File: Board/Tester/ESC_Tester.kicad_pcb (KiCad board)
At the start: 2 copper layers, 40 x 50 mm, 12 parts, among them P1 CONN_01X02, P2 CONN_BLDC, P3 CONN_ISP, P4 CONN_SPI, P5 CONN_PPM, U1 LM7805CT

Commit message: Work in Progress
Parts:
- turned P1 to 270 degrees
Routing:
- net GND: track 21.5 -> 12.1 mm
- net Net-(C1-Pad1): track 30.1 -> 31.6 mm
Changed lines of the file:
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@@
     (links 26)
     (no_connects 0)
-    (area 120.45 48.23736 165.17554 110.33724)
+    (area 120.196 48.23736 165.17554 110.33724)
     (thickness 1.6)
     (drawings 2)
-    (tracks 76)
+    (tracks 77)
     (zones 0)
     (modules 12)
@@
     (pad_to_mask_clearance 0.2)
     (aux_axis_origin 0 0)
-    (visible_elements FFFFFF7F)
+    (visible_elements 7FFFFFFF)
     (pcbplotparams
       (layerselection 0x00000_80000000)
@@
   )
   (module w_conn_kk100:kk100_22-23-2021 (layer F.Cu)
-    (at 126.492 93.98 90)
+    (at 126.492 93.98 270)
     (descr "2 pin vert. connector, Molex KK100 series")
-    (fp_text reference P1 (at 0 -4.318 90) (layer F.SilkS)
-      (effects (font (thickness 0.3048)))
-    )
-    (fp_text value CONN_01X02 (at 0 4.572 90) (layer F.SilkS)
+    (fp_text reference P1 (at 0 -4.318 270) (layer F.SilkS)
+      (effects (font (thickness 0.3048)))
+    )
+    (fp_text value CONN_01X02 (at 0 4.572 270) (layer F.SilkS)
       (effects (font (thickness 0.3048)))
     )
@@
     (fp_line (start -2.54 3.175) (end -2.54 -3.175) (layer F.SilkS) (width 0.254))
     (fp_line (start -2.54 -3.175) (end 2.54 -3.175) (layer F.SilkS) (width 0.254))
-    (pad 1 thru_hole rect (at -1.27 -0.0762 90) (size 1.524 2.1971) (drill 1.016) (layers *.Cu *.Mask F.SilkS)
+    (pad 1 thru_hole rect (at -1.27 -0.0762 270) (size 1.524 2.1971) (drill 1.016) (layers *.Cu *.Mask F.SilkS)
       (net 1 "Net-(C1-Pad1)"))
-    (pad 2 thru_hole oval (at 1.27 -0.0762 90) (size 1.524 2.1971) (drill 1.016) (layers *.Cu *.Mask F.SilkS)
+    (pad 2 thru_hole oval (at 1.27 -0.0762 270) (size 1.524 2.1971) (drill 1.016) (layers *.Cu *.Mask F.SilkS)
       (net 2 GND))
     (model walter/conn_kk100/22-23-2021.wrl
@@
     (effects (font (size 1.5 1.5) (thickness 0.3)) (justify mirror))
   )
-  (gr_text + (at 126.238 99.06) (layer B.Cu)
+  (gr_text + (at 125.222 89.154) (layer B.Cu)
     (effects (font (size 3 3) (thickness 0.5)) (justify mirror))
   )
+  (segment (start 126.5682 92.71) (end 129.794 92.71) (width 0.5) (layer B.Cu) (net 1) (status 400000))
+  (segment (start 132.064 94.98) (end 135.636 94.98) (width 0.5) (layer B.Cu) (net 1) (status 800000))
+  (segment (start 129.794 92.71) (end 132.064 94.98) (width 0.5) (layer B.Cu) (net 1))
+  (segment (start 126.9398 92.726) (end 126.6698 92.456) (width 0.25) (layer F.Cu) (net 1) (status 30))
   (segment (start 152.908 99.06) (end 149.86 99.06) (width 0.5) (layer B.Cu) (net 1))
   (segment (start 149.86 99.06) (end 147.828 97.028) (width 0.5) (layer B.Cu) (net 1))
@@
   (segment (start 135.636 94.98) (end 137.398 94.98) (width 0.5) (layer B.Cu) (net 1))
   (segment (start 137.398 94.98) (end 141.224 98.806) (width 0.5) (layer B.Cu) (net 1))
-  (segment (start 126.4158 95.25) (end 135.366 95.25) (width 0.5) (layer B.Cu) (net 1))
   (segment (start 135.366 95.25) (end 135.636 94.98) (width 0.5) (layer B.Cu) (net 1))
   (segment (start 135.239 94.996) (end 135.509 94.726) (width 0.25) (layer F.Cu) (net 1) (status 30))
@@
   (via (at 154.432 61.468) (size 1.5) (drill 0.8) (layers F.Cu B.Cu) (net 2))
   (segment (start 155.956 62.992) (end 154.432 61.468) (width 0.5) (layer B.Cu) (net 2))
-  (segment (start 126.4158 92.71) (end 135.366 92.71) (width 0.5) (layer B.Cu) (net 2))
   (segment (start 135.366 92.71) (end 135.636 92.98) (width 0.5) (layer B.Cu) (net 2))
   (segment (start 158.266 93.559) (end 158.623 93.202) (width 0.25) (layer F.Cu) (net 2) (status 30))
-  (segment (start 126.9398 92.726) (end 126.6698 92.456) (width 0.25) (layer F.Cu) (net 2) (status 30))
   (segment (start 142.24 62.484) (end 136.144 62.484) (width 0.5) (layer B.Cu) (net 3))
   (segment (start 153.924 85.852) (end 159.004 90.932) (width 0.5) (layer B.Cu) (net 3))
@@
   (segment (start 141.986 91.948) (end 141.224 91.186) (width 0.5) (layer B.Cu) (net 3))
   (segment (start 158.48 91.059) (end 158.623 91.202) (width 0.25) (layer F.Cu) (net 3) (status 30))
-  (segment (start 155.956 77.64526) (end 138.50874 77.64526) (width 0.3) (layer B.Cu) (net 4) (status 400000))
-  (segment (start 133.096 83.058) (end 129.032 83.058) (width 0.3) (layer B.Cu) (net 4) (status 800000))
+  (segment (start 155.956 77.64526) (end 138.50874 77.64526) (width 0.3) (layer B.Cu) (net 4))
+  (segment (start 133.096 83.058) (end 129.032 83.058) (width 0.3) (layer B.Cu) (net 4))
   (segment (start 138.50874 77.64526) (end 133.096 83.058) (width 0.3) (layer B.Cu) (net 4))
   (segment (start 155.956 75.64374) (end 133.65226 75.64374) (width 0.3) (layer B.Cu) (net 5))

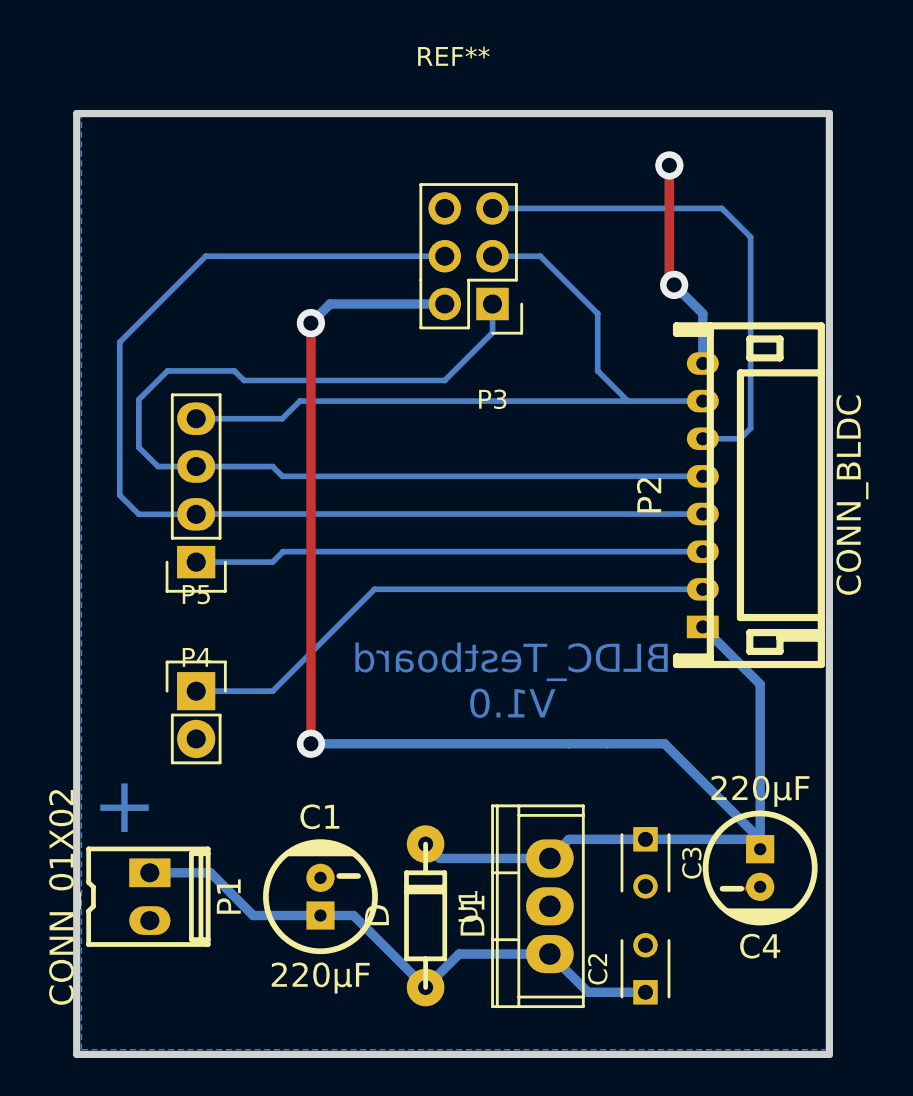
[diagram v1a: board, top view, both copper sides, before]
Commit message: BOM erzeugt, Testerboard layout
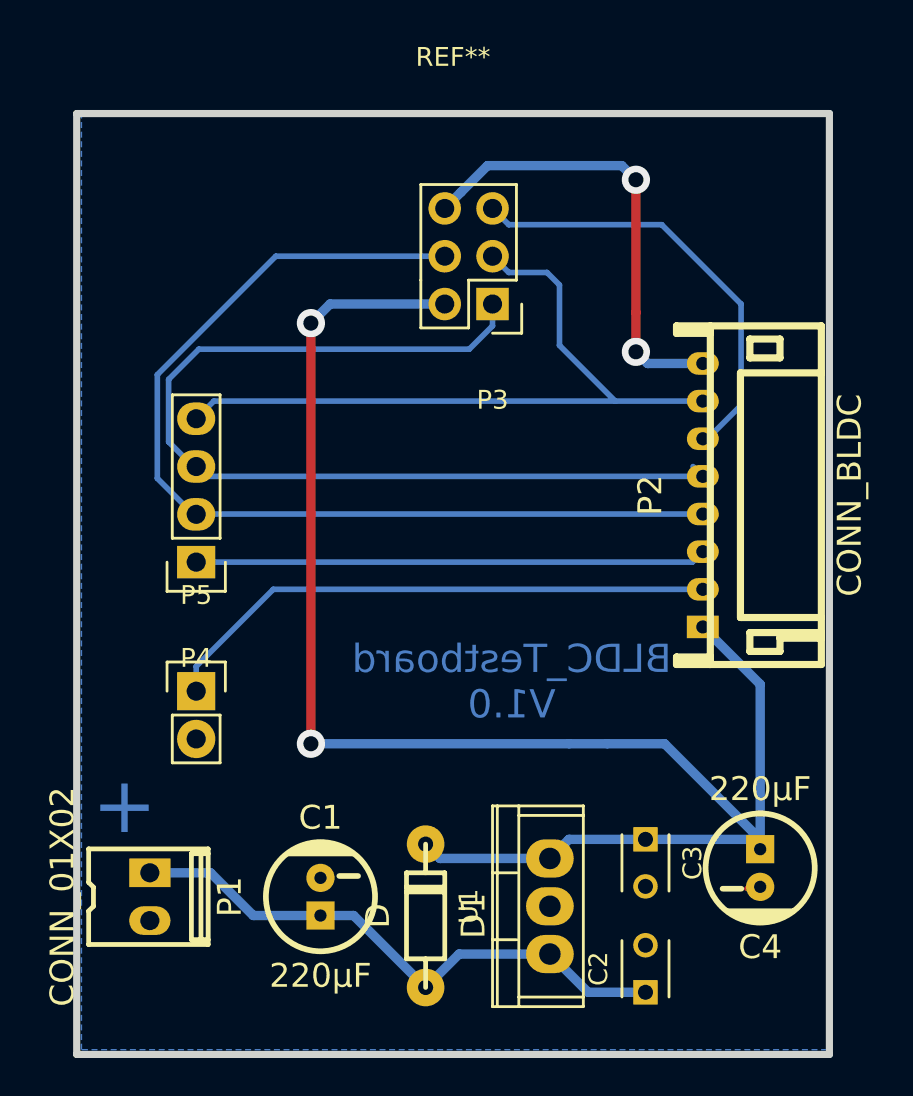
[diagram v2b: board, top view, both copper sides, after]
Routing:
- net GND: track 12.1 -> 25.3 mm
- net /MOSI: track 58.7 -> 53.2 mm
- net /Reset: track 27.3 -> 23.5 mm
- net /MISO: track 55.4 -> 53.4 mm
- net /PPM: track 29.2 -> 29.9 mm
- net /SCK: track 39.5 -> 38.9 mm
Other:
- net class 5V: clearance 0.2 -> 0.3
- net class Default: clearance 0.2 -> 0.3
- net class Sup: clearance 0.2 -> 0.3
- rule trace_clearance: 0.2 -> 0.3

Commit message: Work in Progress
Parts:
- P2: footprint w_conn_jst-ph:s8b-ph-kl -> Connectors_Molex:Connector_Molex_PicoBlade_53261-0871
- moved P2 4.57 mm to (160.5, 72.6)
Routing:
- net GND: track 25.3 -> 0.00 mm, vias 2 -> 0
- net /MOSI: track 53.2 -> 58.8 mm
- net /MISO: track 53.4 -> 57.4 mm
- net /Reset: track 23.5 -> 25.8 mm, vias 0 -> 2
- net /SS: track 27.2 -> 29.4 mm
- net /PPM: track 29.9 -> 31.6 mm
- net +5V: track 88.4 -> 86.8 mm
- net /SCK: track 38.9 -> 40.4 mm
- net Net-(C1-Pad1): track 31.6 -> 30.4 mm
- added copper zone on F.Cu, net GND
- removed copper zone on B.Cu, net GND
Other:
- board text added: "ESC_Testboard V1.0"
- board text removed: "BLDC_Testboard V1.0"
